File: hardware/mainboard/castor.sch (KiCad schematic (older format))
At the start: 41 parts, among them Q1 MMBT3904, U3 TL074, U4 74LVC2G74, U5 MCP6001-OT, U6 TL074

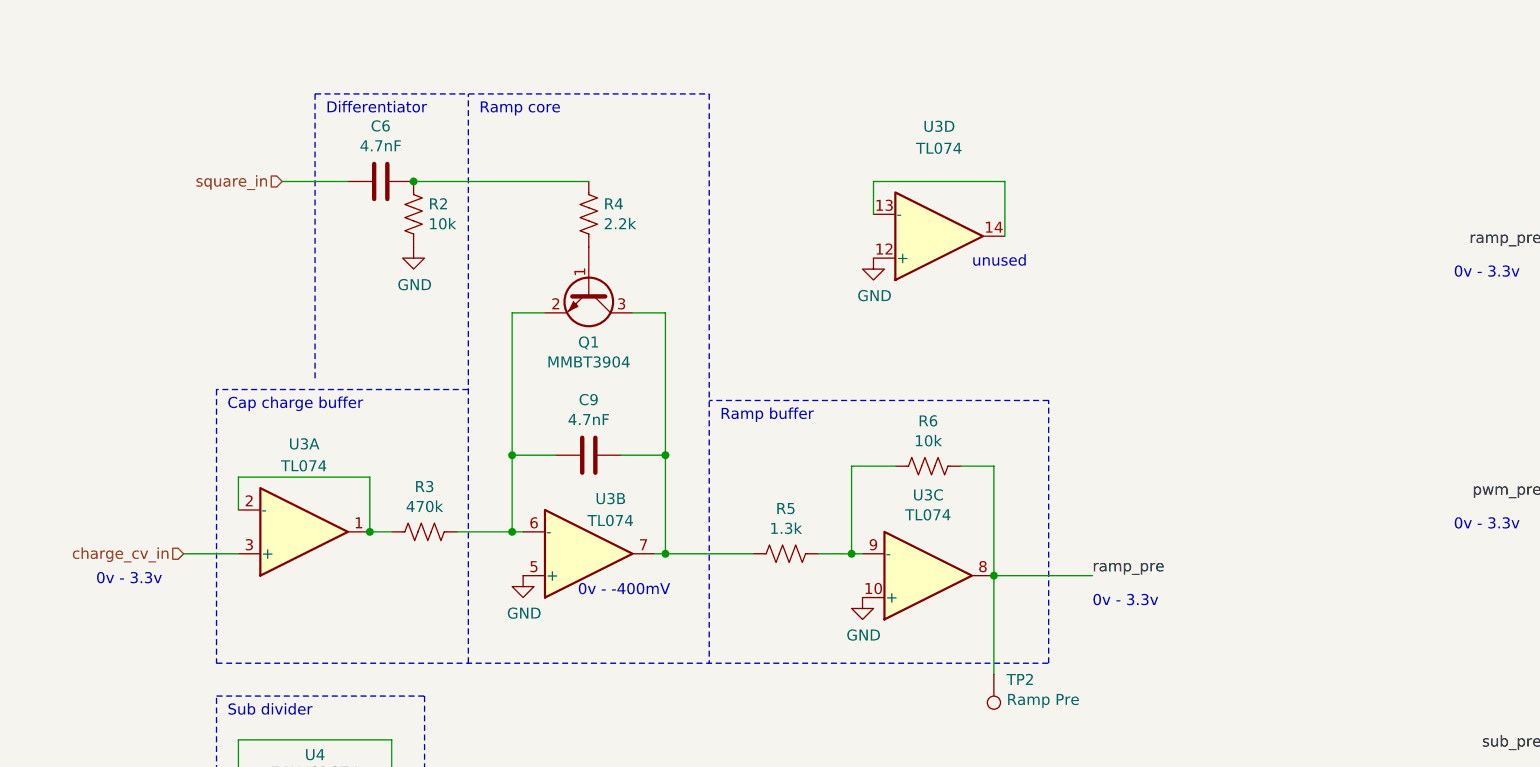
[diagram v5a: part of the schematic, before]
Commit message: Create hardware revision mainboard v3
This addresses an issue with the ramp oscillators using the wrong type of transistor.
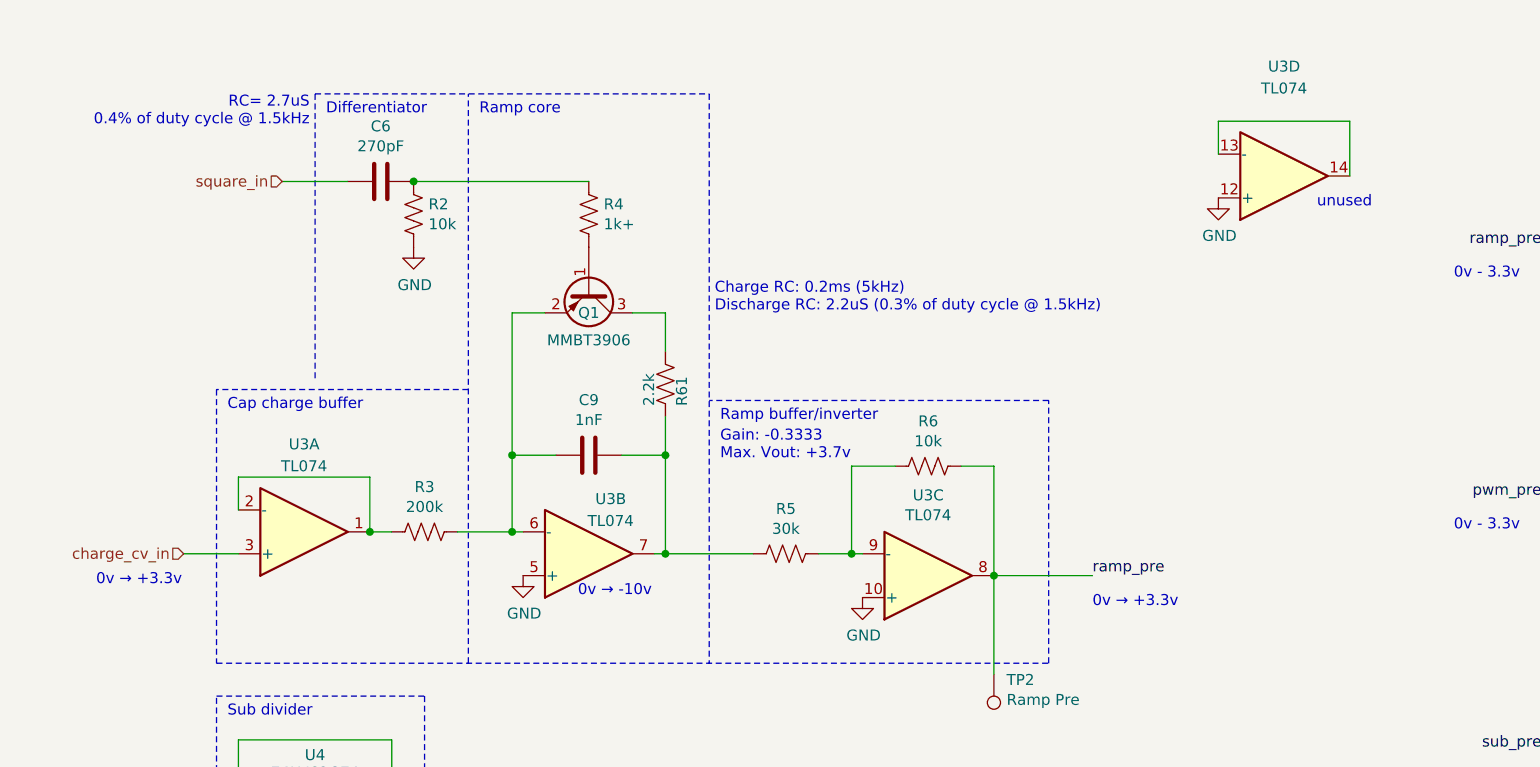
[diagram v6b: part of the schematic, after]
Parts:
- removed Q1: MMBT3904, Package_TO_SOT_SMD:SOT-23, symbol Transistor_BJT:MMBT3904
- added Q1: MMBT3906, Package_TO_SOT_SMD:SOT-23, symbol Transistor_BJT:MMBT3906
- added R61: 2.2k, Resistor_SMD:R_0603_1608Metric_Pad1.05x0.95mm_HandSolder, symbol Device:R_US
- C6: value 4.7nF -> 270pF; mpn C0603C472F3GECTU -> GCM1885C2A271FA16D; mpn alt C0603C472F5GACTU -> GRM1885C2A271JA01D
- C9: value 4.7nF -> 1nF; mpn C0603C472F3GECTU -> GRM1885C1H102FA01J; mpn alt C0603C472F5GACTU -> GRM1885C1H102FA01D
- R3: value 470k -> 200k; Reqs 0.5% -> 5%; mpn ERA-6AEB474V -> ERA-3AEB204V
- R4: value 2.2k -> 1k+; Reqs (none) -> 1k+, needs testing; finalized yes -> (none); mpn ERA-3AED222V -> ERA-3AED102V
- R5: value 1.3k -> 30k; Reqs 0.5% -> 1%; mpn ERA-3AEB132V -> RR0816P-303-D; mpn alt (none) -> ERA-3AEB303V
- R6: Reqs 1% -> 5%
- TP2: dnp (none) -> 1; finalized (none) -> yes
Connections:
- net at R4.1: now also Q1.1 (B)
- net at C9.2, R3.2, U3.6 (-): now also Q1.2 (E)
- net at C9.1, R5.1, U3.7: now also R61.1
- new net: Q1.3 (C), R61.2
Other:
- note added: "0v → +3.3v"
- note added: "0v → -10v"
- note added: "Charge RC: 0.2ms (5kHz)\nDischarge RC: 2.2uS (0.3% of duty cycle @ 1.5kHz)"
- note added: "Gain: -0.3333\nMax. Vout: +3.7v"
- note added: "RC= 2.7uS\n0.4% of duty cycle @ 1.5kHz"
- note added: "Ramp buffer/inverter\n"
- note removed: "0v - -400mV"
- note removed: "Ramp buffer\n"
- moved on the sheet: U3D
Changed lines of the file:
@@
 Sheet 7 7
 Title "Castor & Pollux"
-Date "2020-09-26"
-Rev "v2"
+Date "2021-01-27"
+Rev "v3"
 Comp "Winterbloom"
 Comment1 "CERN-OHL-P v2"
@@
 AR Path="/5F0E55E2/5EE545BA" Ref="C25"  Part="1"
 F 0 "C6" V 2098 1250 50  0000 C CNN
-F 1 "4.7nF" V 2189 1250 50  0000 C CNN
+F 1 "270pF" V 2189 1250 50  0000 C CNN
 F 2 "Capacitor_SMD:C_0603_1608Metric_Pad1.05x0.95mm_HandSolder" H 2388 1100 50  0001 C CNN
 F 3 "~" H 2350 1250 50  0001 C CNN
 F 4 "C0G 1%" H 2350 1250 50  0001 C CNN "Reqs"
 F 5 "yes" H 2350 1250 50  0001 C CNN "finalized"
-F 6 "C0603C472F3GECTU" H 2350 1250 50  0001 C CNN "mpn"
+F 6 "GCM1885C2A271FA16D" H 2350 1250 50  0001 C CNN "mpn"
 F 7 "1%, 50v" H 2350 1250 50  0001 C CNN "mpn specs"
-F 8 "C0603C472F5GACTU" H 2350 1250 50  0001 C CNN "mpn alt"
+F 8 "GRM1885C2A271JA01D" H 2350 1250 50  0001 C CNN "mpn alt"
 	1    2350 1250
 	0    1    1    0
@@
 AR Path="/5F0E55E2/5EE54BED" Ref="R28"  Part="1"
 F 0 "R4" H 3232 1354 50  0000 R CNN
-F 1 "2.2k" H 3232 1445 50  0000 R CNN
+F 1 "1k+" H 3232 1445 50  0000 R CNN
 F 2 "Resistor_SMD:R_0603_1608Metric_Pad1.05x0.95mm_HandSolder" V 3340 1390 50  0001 C CNN
 F 3 "~" H 3300 1400 50  0001 C CNN
-F 4 "yes" H 3300 1400 50  0001 C CNN "finalized"
-F 5 "ERA-3AED222V" H 3300 1400 50  0001 C CNN "mpn"
+F 4 "" H 3300 1400 50  0001 C CNN "finalized"
+F 5 "ERA-3AED102V" H 3300 1400 50  0001 C CNN "mpn"
 F 6 "100mW" H 3300 1400 50  0001 C CNN "mpn specs"
+F 7 "1k+, needs testing" H 3300 1400 50  0001 C CNN "Reqs"
 	1    3300 1400
 	-1   0    0    1
@@
 AR Path="/5F0E55E2/5EE5D698" Ref="C28"  Part="1"
 F 0 "C9" V 3048 2500 50  0000 C CNN
-F 1 "4.7nF" V 3139 2500 50  0000 C CNN
+F 1 "1nF" V 3139 2500 50  0000 C CNN
 F 2 "Capacitor_SMD:C_0603_1608Metric_Pad1.05x0.95mm_HandSolder" H 3338 2350 50  0001 C CNN
 F 3 "~" H 3300 2500 50  0001 C CNN
 F 4 "C0G 1%" H 3300 2500 50  0001 C CNN "Reqs"
 F 5 "yes" H 3300 2500 50  0001 C CNN "finalized"
-F 6 "C0603C472F3GECTU" H 3300 2500 50  0001 C CNN "mpn"
+F 6 "GRM1885C1H102FA01J" H 3300 2500 50  0001 C CNN "mpn"
 F 7 "1%, 50v" H 3300 2500 50  0001 C CNN "mpn specs"
-F 8 "C0603C472F5GACTU" H 3300 2500 50  0001 C CNN "mpn alt"
+F 8 "GRM1885C1H102FA01D" H 3300 2500 50  0001 C CNN "mpn alt"
 	1    3300 2500
 	0    1    1    0
@@
 Wire Wire Line
 	3450 2500 3650 2500
-Wire Wire Line
-	3650 2500 3650 1850
 Wire Wire Line
 	3650 1850 3500 1850
@@
 AR Path="/5F0E55E2/5EE67C3A" Ref="R27"  Part="1"
 F 0 "R3" V 2755 2850 50  0000 C CNN
-F 1 "470k" V 2664 2850 50  0000 C CNN
+F 1 "200k" V 2664 2850 50  0000 C CNN
 F 2 "Resistor_SMD:R_0805_2012Metric_Pad1.15x1.40mm_HandSolder" V 2590 2840 50  0001 C CNN
 F 3 "~" H 2550 2850 50  0001 C CNN
 F 4 "yes" H 2550 2850 50  0001 C CNN "finalized"
-F 5 "ERA-6AEB474V" H 2550 2850 50  0001 C CNN "mpn"
-F 6 "0.5%" H 2550 2850 50  0001 C CNN "Reqs"
+F 5 "ERA-3AEB204V" H 2550 2850 50  0001 C CNN "mpn"
+F 6 "5%" H 2550 2850 50  0001 C CNN "Reqs"
 F 7 "100mW" H 2550 2850 50  0001 C CNN "mpn specs"
 	1    2550 2850
@@
 Ramp core
 Text Notes 1050 3100 0    50   ~ 0
-0v - 3.3v
-$Comp
-L Device:R_US R5
-U 1 1 5EE6F81D
-P 4200 2950
-AR Path="/5F016AD7/5EE6F81D" Ref="R5"  Part="1"
-AR Path="/5F0E55E2/5EE6F81D" Ref="R29"  Part="1"
-F 0 "R5" V 4405 2950 50  0000 C CNN
-F 1 "1.3k" V 4314 2950 50  0000 C CNN
-F 2 "Resistor_SMD:R_0603_1608Metric_Pad1.05x0.95mm_HandSolder" V 4240 2940 50  0001 C CNN
-F 3 "~" H 4200 2950 50  0001 C CNN
-F 4 "yes" H 4200 2950 50  0001 C CNN "finalized"
-F 5 "ERA-3AEB132V" H 4200 2950 50  0001 C CNN "mpn"
-F 6 "0.5%" H 4200 2950 50  0001 C CNN "Reqs"
-F 7 "100mW" H 4200 2950 50  0001 C CNN "mpn specs"
-	1    4200 2950
-	0    -1   -1   0
-$EndComp
+0v → +3.3v
 $Comp
 L Amplifier_Operational:TL074 U3
@@
 F 4 "yes" H 4850 2550 50  0001 C CNN "finalized"
 F 5 "ERA-3AED103V" H 4850 2550 50  0001 C CNN "mpn"
-F 6 "1%" H 4850 2550 50  0001 C CNN "Reqs"
+F 6 "5%" H 4850 2550 50  0001 C CNN "Reqs"
 F 7 "100mW" H 4850 2550 50  0001 C CNN "mpn specs"
 	1    4850 2550
@@
 	5150 2550 5150 3050
 Text Notes 3250 3150 0    50   ~ 0
-0v - -400mV
+0v → -10v
 Text Notes 5600 3200 0    50   ~ 0
-0v - 3.3v
+0v → +3.3v
 Wire Notes Line
 	3850 850  3850 3450
 Text Notes 3900 2350 0    50   ~ 0
-Ramp buffer\n
+Ramp buffer/inverter\n
 Wire Notes Line
 	5400 3450 5400 2250
@@
 Wire Wire Line
 	3650 2500 3650 2950
-Connection ~ 3650 2500
 Connection ~ 3650 2950
 Wire Wire Line
@@
 	1    1900 4450
 	1    0    0    -1
-$EndComp
-$Comp
-L Transistor_BJT:MMBT3904 Q1
-U 1 1 5F14584B
-P 3300 1750
-AR Path="/5F016AD7/5F14584B" Ref="Q1"  Part="1"
-AR Path="/5F0E55E2/5F14584B" Ref="Q2"  Part="1"
-F 0 "Q1" V 3535 1750 50  0000 C CNN
-F 1 "MMBT3904" V 3626 1750 50  0000 C CNN
-F 2 "Package_TO_SOT_SMD:SOT-23" H 3500 1675 50  0001 L CIN
-F 3 "https://www.fairchildsemi.com/datasheets/2N/2N3904.pdf" H 3300 1750 50  0001 L CNN
-F 4 "yes" H 3300 1750 50  0001 C CNN "finalized"
-F 5 "MF-DSC-SOT233-MMBT3904" H 3300 1750 50  0001 C CNN "mpn"
-F 6 "MMBT3904,215" H 3300 1750 50  0001 C CNN "mpn alt"
-	1    3300 1750
-	0    1    1    0
 $EndComp
 Text HLabel 1900 1250 0    50   Input ~ 0
@@
 L Amplifier_Operational:TL074 U3
 U 4 1 5F103946
-P 4900 1500
+P 6475 1225
 AR Path="/5F016AD7/5F103946" Ref="U3"  Part="4"
 AR Path="/5F0E55E2/5F103946" Ref="U9"  Part="4"
-F 0 "U3" H 4900 1000 50  0000 C CNN
-F 1 "TL074" H 4900 1100 50  0000 C CNN
-F 2 "Package_SO:TSSOP-14_4.4x5mm_P0.65mm" H 4850 1600 50  0001 C CNN
-F 3 "http://www.ti.com/lit/ds/symlink/tl071.pdf" H 4950 1700 50  0001 C CNN
-F 4 "yes" H 4900 1500 50  0001 C CNN "finalized"
-F 5 "TL074CPWR" H 4900 1500 50  0001 C CNN "mpn"
-	4    4900 1500
+F 0 "U3" H 6475 725 50  0000 C CNN
+F 1 "TL074" H 6475 825 50  0000 C CNN
+F 2 "Package_SO:TSSOP-14_4.4x5mm_P0.65mm" H 6425 1325 50  0001 C CNN
+F 3 "http://www.ti.com/lit/ds/symlink/tl071.pdf" H 6525 1425 50  0001 C CNN
+F 4 "yes" H 6475 1225 50  0001 C CNN "finalized"
+F 5 "TL074CPWR" H 6475 1225 50  0001 C CNN "mpn"
+	4    6475 1225
 	1    0    0    1
 $EndComp
@@
 L power:GND #PWR036
 U 1 1 5F105CB5
-P 4600 1600
+P 6175 1325
 AR Path="/5F016AD7/5F105CB5" Ref="#PWR036"  Part="1"
 AR Path="/5F0E55E2/5F105CB5" Ref="#PWR093"  Part="1"
-F 0 "#PWR036" H 4600 1350 50  0001 C CNN
-F 1 "GND" H 4605 1427 50  0000 C CNN
-F 2 "" H 4600 1600 50  0001 C CNN
-F 3 "" H 4600 1600 50  0001 C CNN
-	1    4600 1600
-	1    0    0    -1
-$EndComp
-Wire Wire Line
-	5200 1500 5200 1250
-Wire Wire Line
-	5200 1250 4600 1250
-Wire Wire Line
-	4600 1250 4600 1400
+F 0 "#PWR036" H 6175 1075 50  0001 C CNN
+F 1 "GND" H 6180 1152 50  0000 C CNN
+F 2 "" H 6175 1325 50  0001 C CNN
+F 3 "" H 6175 1325 50  0001 C CNN
+	1    6175 1325
+	1    0    0    -1
+$EndComp
+Wire Wire Line
+	6775 1225 6775 975
+Wire Wire Line
+	6775 975  6175 975
+Wire Wire Line
+	6175 975  6175 1125
 Wire Wire Line
 	7150 4800 7850 4800
@@
 Wire Wire Line
 	7150 6200 7850 6200
-Text Notes 5050 1650 0    50   ~ 0
+Text Notes 6625 1375 0    50   ~ 0
 unused
 Wire Wire Line
@@
 F 2 "TestPoint:TestPoint_Pad_D1.0mm" H 5350 3500 50  0001 C CNN
 F 3 "~" H 5350 3500 50  0001 C CNN
+F 4 "1" H 5150 3500 50  0001 C CNN "dnp"
+F 5 "yes" H 5150 3500 50  0001 C CNN "finalized"
 	1    5150 3500
 	-1   0    0    1
@@
 Wire Wire Line
 	9550 5600 9800 5600
+$Comp
+L Transistor_BJT:MMBT3906 Q1
+U 1 1 601956FB
+P 3300 1750
+AR Path="/5F016AD7/601956FB" Ref="Q1"  Part="1"
+AR Path="/5F0E55E2/601956FB" Ref="Q2"  Part="1"
+F 0 "Q1" V 3400 1750 50  0000 C CNN
+F 1 "MMBT3906" V 3525 1750 50  0000 C CNN
+F 2 "Package_TO_SOT_SMD:SOT-23" H 3500 1675 50  0001 L CIN
+F 3 "https://www.fairchildsemi.com/datasheets/2N/2N3906.pdf" H 3300 1750 50  0001 L CNN
+F 4 "yes" H 3300 1750 50  0001 C CNN "finalized"
+F 5 "MF-DSC-SOT233-MMBT3906" H 3300 1750 50  0001 C CNN "mpn"
+F 6 "MMBT3906L" H 3300 1750 50  0001 C CNN "mpn alt"
+	1    3300 1750
+	0    1    1    0
+$EndComp
+$Comp
+L Device:R_US R61
+U 1 1 6019886A
+P 3650 2175
+AR Path="/5F016AD7/6019886A" Ref="R61"  Part="1"
+AR Path="/5F0E55E2/6019886A" Ref="R60"  Part="1"
+F 0 "R61" V 3575 2275 50  0000 R CNN
+F 1 "2.2k" V 3725 2275 50  0000 R CNN
+F 2 "Resistor_SMD:R_0603_1608Metric_Pad1.05x0.95mm_HandSolder" V 3690 2165 50  0001 C CNN
+F 3 "~" H 3650 2175 50  0001 C CNN
+F 4 "yes" H 3650 2175 50  0001 C CNN "finalized"
+F 5 "ERA-3AED222V" H 3650 2175 50  0001 C CNN "mpn"
+F 6 "100mW" H 3650 2175 50  0001 C CNN "mpn specs"
+F 7 "1%" H 3650 2175 50  0001 C CNN "Reqs"
+	1    3650 2175
+	-1   0    0    1
+$EndComp
+Wire Wire Line
+	3650 1850 3650 2025
+Wire Wire Line
+	3650 2325 3650 2500
+Connection ~ 3650 2500
+Text Notes 2025 1000 2    50   ~ 0
+RC= 2.7uS\n0.4% of duty cycle @ 1.5kHz
+Text Notes 3875 1850 0    50   ~ 0
+Charge RC: 0.2ms (5kHz)\nDischarge RC: 2.2uS (0.3% of duty cycle @ 1.5kHz)
+Text Notes 3900 2525 0    50   ~ 0
+Gain: -0.3333\nMax. Vout: +3.7v
+$Comp
+L Device:R_US R5
+U 1 1 5EE6F81D
+P 4200 2950
+AR Path="/5F016AD7/5EE6F81D" Ref="R5"  Part="1"
+AR Path="/5F0E55E2/5EE6F81D" Ref="R29"  Part="1"
+F 0 "R5" V 4405 2950 50  0000 C CNN
+F 1 "30k" V 4314 2950 50  0000 C CNN
+F 2 "Resistor_SMD:R_0603_1608Metric_Pad1.05x0.95mm_HandSolder" V 4240 2940 50  0001 C CNN
+F 3 "~" H 4200 2950 50  0001 C CNN
+F 4 "yes" H 4200 2950 50  0001 C CNN "finalized"
+F 5 "RR0816P-303-D" H 4200 2950 50  0001 C CNN "mpn"
+F 6 "1%" H 4200 2950 50  0001 C CNN "Reqs"
+F 7 "100mW" H 4200 2950 50  0001 C CNN "mpn specs"
+F 8 "ERA-3AEB303V" H 4200 2950 50  0001 C CNN "mpn alt"
+	1    4200 2950
+	0    -1   -1   0
+$EndComp
 $EndSCHEMATC

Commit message: hardware: finalize BOM for v3, change 200kOhm resistors to 0603.
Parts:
- R3: footprint Resistor_SMD:R_0805_2012Metric_Pad1.15x1.40mm_HandSolder -> Resistor_SMD:R_0603_1608Metric_Pad1.05x0.95mm_HandSolder
- R4: finalized (none) -> yes; mpn ERA-3AED102V -> ERA-3AEB102V
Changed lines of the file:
@@
 Sheet 7 7
 Title "Castor & Pollux"
-Date "2021-01-27"
+Date "2021-02-01"
 Rev "v3"
 Comp "Winterbloom"
@@
 F 2 "Resistor_SMD:R_0603_1608Metric_Pad1.05x0.95mm_HandSolder" V 3340 1390 50  0001 C CNN
 F 3 "~" H 3300 1400 50  0001 C CNN
-F 4 "" H 3300 1400 50  0001 C CNN "finalized"
-F 5 "ERA-3AED102V" H 3300 1400 50  0001 C CNN "mpn"
+F 4 "yes" H 3300 1400 50  0001 C CNN "finalized"
+F 5 "ERA-3AEB102V" H 3300 1400 50  0001 C CNN "mpn"
 F 6 "100mW" H 3300 1400 50  0001 C CNN "mpn specs"
 F 7 "1k+, needs testing" H 3300 1400 50  0001 C CNN "Reqs"
@@
 F 0 "R3" V 2755 2850 50  0000 C CNN
 F 1 "200k" V 2664 2850 50  0000 C CNN
-F 2 "Resistor_SMD:R_0805_2012Metric_Pad1.15x1.40mm_HandSolder" V 2590 2840 50  0001 C CNN
+F 2 "Resistor_SMD:R_0603_1608Metric_Pad1.05x0.95mm_HandSolder" V 2590 2840 50  0001 C CNN
 F 3 "~" H 2550 2850 50  0001 C CNN
 F 4 "yes" H 2550 2850 50  0001 C CNN "finalized"

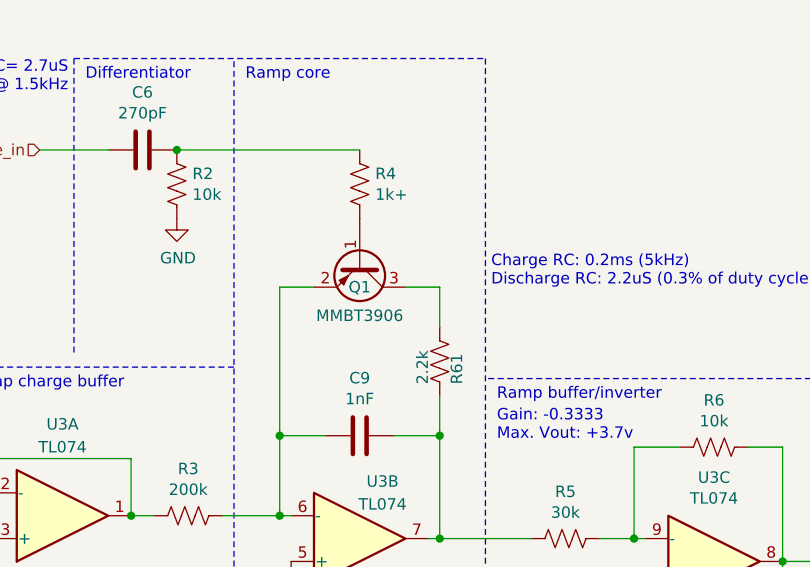
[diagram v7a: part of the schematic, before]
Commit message: hardware: finalize v3 of mainboard for production
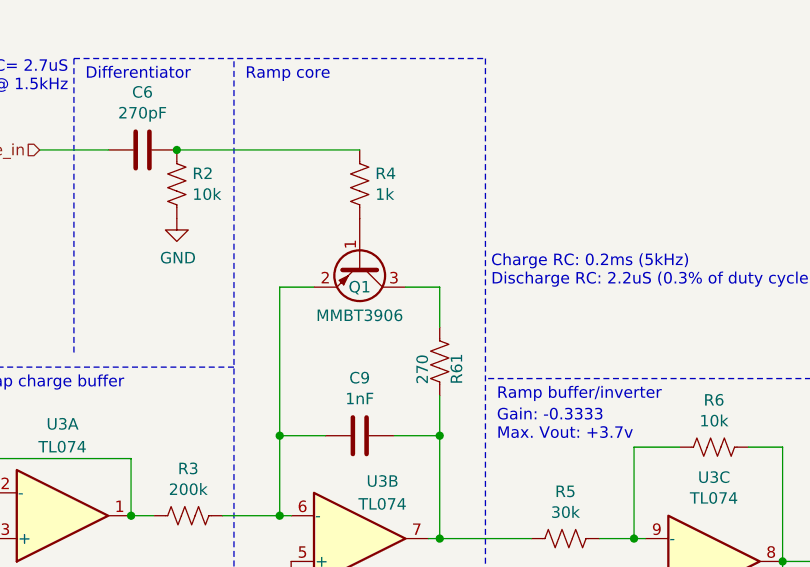
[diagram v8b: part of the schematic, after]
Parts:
- C10, C5, C7, C8: Reqs (none) -> bypass
- C11, C12, C13: Reqs (none) -> audio path; mpn GRM21BR61E106KA73K -> CL21A106KAYNNNG; mpn alt (none) -> GRM21BR61E106KA73K
- C14, C15, C16: Reqs (none) -> audio filter
- C17: Reqs (none) -> audio filter; mpn GCM1885C2A8R2DA16D -> GRM1885C1H8R2WA01D; mpn alt (none) -> GCM1885C2A8R2DA16D
- C6: mpn GCM1885C2A271FA16D -> GRM1885C2A271JA01D; mpn alt GRM1885C2A271JA01D -> (none)
- R10, R11, R12: Reqs 0.5% -> 1%, audio path; mpn ERA-3AED473V -> RR0816P-473-D; mpn alt (none) -> ERA-3AED473V
- R13, R14, R15: Reqs 1% -> 1%, audio path; mpn ERA-3AED103V -> RR0816P-103-D; mpn alt (none) -> ERA-3AED103V
- R16, R17, R18: Reqs 0.5% -> 1%, audio path; mpn ERA-3AEB3652V -> RR0816P-3652-D-55C; mpn alt (none) -> ERA-3AEB3652V
- R19, R7, R8, R9: Reqs 0.5% -> 1%, audio path; mpn ERA-3AED104V -> RR0816P-104-D; mpn alt (none) -> ERA-3AED104V
- R2: Reqs 1% -> 1%, control path; mpn ERA-3AED103V -> RR0816P-103-D; mpn alt (none) -> ERA-3AED103V
- R20, R21, R22, R23: Reqs thin film -> 5%, audio path; mpn ERA-3AED102V -> RR0816P-102-D; mpn alt (none) -> ERA-3AEB102V
- R3: Reqs 5% -> 5%, control path; mpn ERA-3AEB204V -> RR0816P-204-D; mpn alt (none) -> ERA-3AEB204V
- R4: value 1k+ -> 1k; Reqs 1k+, needs testing -> 5%, control path; mpn ERA-3AEB102V -> RR0816P-102-D; mpn alt (none) -> ERA-3AEB102V
- R5: Reqs 1% -> 1%, audio path
- R6: Reqs 5% -> 1%, audio path; mpn ERA-3AED103V -> RR0816P-103-D; mpn alt (none) -> ERA-3AED103V
- R61: value 2.2k -> 270; mpn ERA-3AED222V -> RR0816P-271-D
